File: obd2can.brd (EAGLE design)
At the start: 34.6 x 29.1 mm, 18 parts, among them Q1 16MHz, SW3 6X3.5_TACT, U2 SN65HVD235DR, U3 STM32F030XTSSOP20, U4 MCP1700, X1 RJ45_RIGHT_ANGLEMOLEX_95001-2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

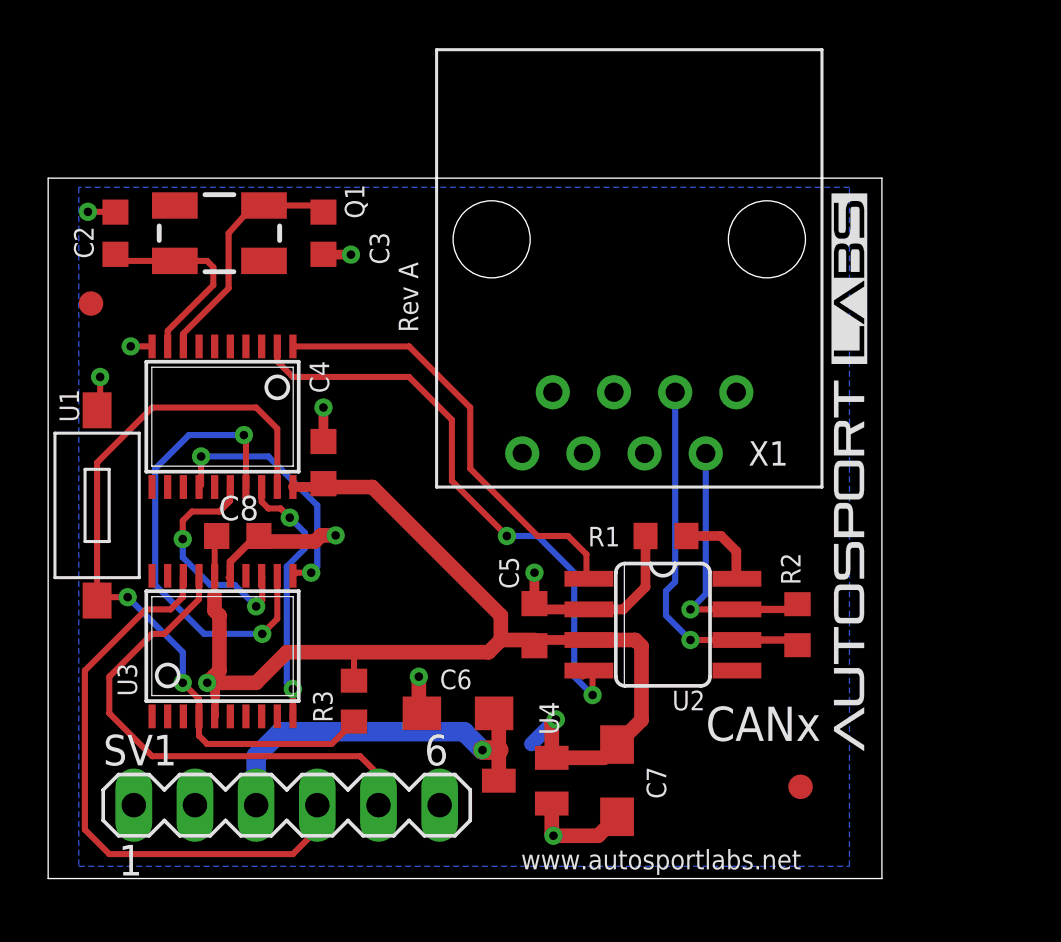
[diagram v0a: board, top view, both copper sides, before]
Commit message: added swdebug and boot button
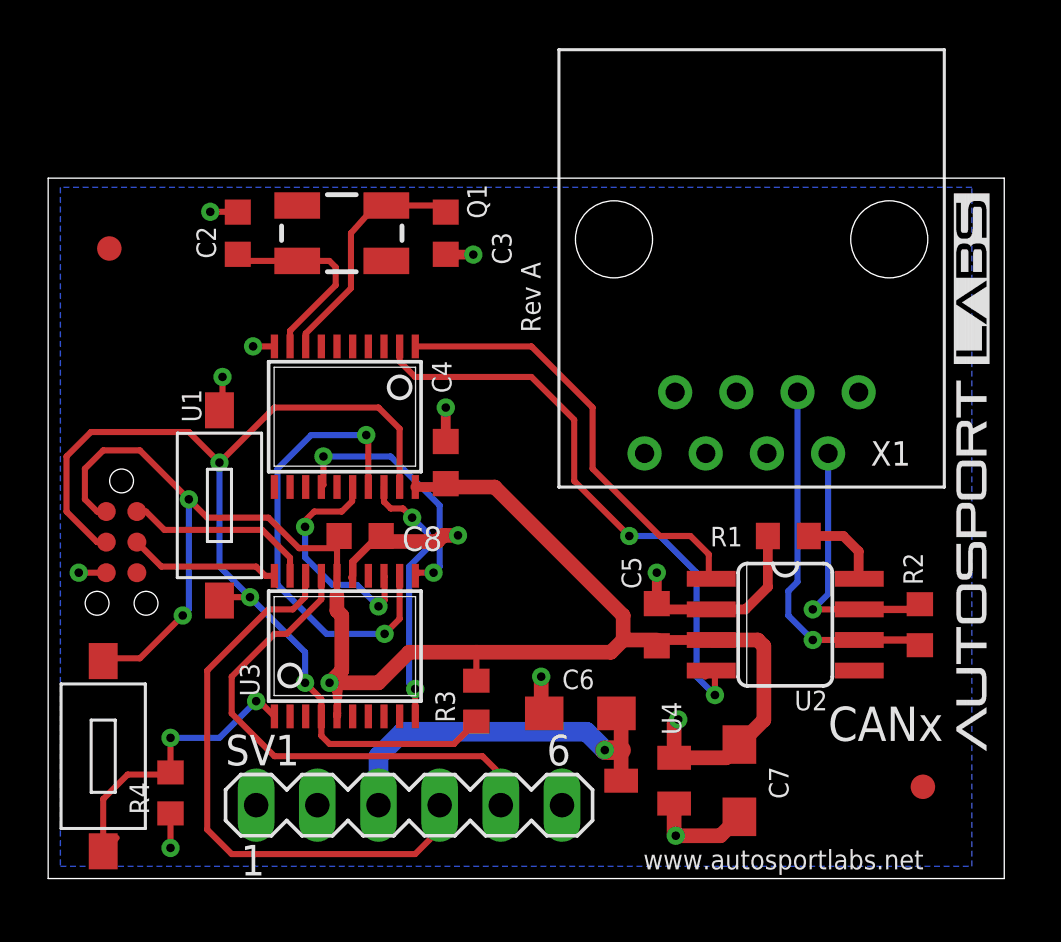
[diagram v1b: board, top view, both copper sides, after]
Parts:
- added R4: 4.7K, rcl:R0603
- added SW1: 6X3.5_TACT, tactile_switch:TACT_6X3.5
- added TC1: TC2030-IDC-NL, TagConnect:TC2030-IDC-NL
- moved C3 5.08 mm to (16.5, 26.8)
- moved C4 5.08 mm to (16.5, 17.3)
- moved C7 5.08 mm to (28.7, 4.06)
- moved R1 5.08 mm to (30.7, 14.2)
- moved R2 5.08 mm to (36.2, 10.5)
- moved R3 5.08 mm to (17.8, 7.37)
- moved X1 5.08 mm to (29.2, 26.5)
- moved C8 5.08 mm to (13.0, 14.2)
- moved U1 5.08 mm to (12.3, 19.2)
- moved U3 5.08 mm to (12.3, 9.65)
- moved C2 5.08 mm to (7.87, 26.8)
- moved Q1 5.08 mm to (12.2, 26.8)
- moved SV1 5.08 mm to (15.0, 3.05)
- moved SW3 5.08 mm to (7.11, 15.5)
- moved C5 5.08 mm to (25.3, 10.5)
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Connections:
- new net BOOT0: R4.2, SW1.P$1, U3.1
- new net SWCLK: TC1.4, U3.20
- new net SWDIO: TC1.2, U3.19
- net GND: now also R4.1, TC1.5
- net RESET: now also TC1.3
- net V+: now also SW1.P$2, TC1.1
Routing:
- net V+: track 50.9 -> 73.6 mm, vias 2 -> 4
- net BOOT0: track 0.00 -> 12.9 mm, vias 0 -> 2
- net RESET: track 32.2 -> 44.4 mm, vias 2 -> 3
- net SWDIO: track 0.00 -> 7.91 mm
- net SWCLK: track 0.00 -> 6.29 mm
- net GND: track 26.4 -> 29.2 mm, vias 9 -> 11
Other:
- board size 34.6 x 29.1 mm -> 39.7 x 29.1 mm

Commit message: minor label updates
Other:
- board text added: "OBD2CAN"
- board text removed: "CANx"
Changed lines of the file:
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@@
 <wire x1="39.7002" y1="29.083" x2="0" y2="29.083" width="0" layer="20"/>
 <wire x1="0" y1="29.083" x2="0" y2="0" width="0" layer="20"/>
-<text x="24.7142" y="0.381" size="0.8128" layer="21" font="vector">www.autosportlabs.net</text>
+<text x="11.2522" y="0.381" size="0.8128" layer="21" font="vector">www.autosportlabs.net</text>
 <text x="20.447" y="22.6822" size="0.8128" layer="21" font="vector" rot="R90">Rev A</text>
-<text x="32.385" y="5.715" size="1.4224" layer="21">CANx</text>
+<text x="29.845" y="1.397" size="1.4224" layer="21">OBD2CAN</text>
 <rectangle x1="35.5422" y1="24.9022" x2="42.6288" y2="24.9148" layer="21" rot="R90"/>
 <rectangle x1="35.5295" y1="24.9022" x2="42.6161" y2="24.9148" layer="21" rot="R90"/>

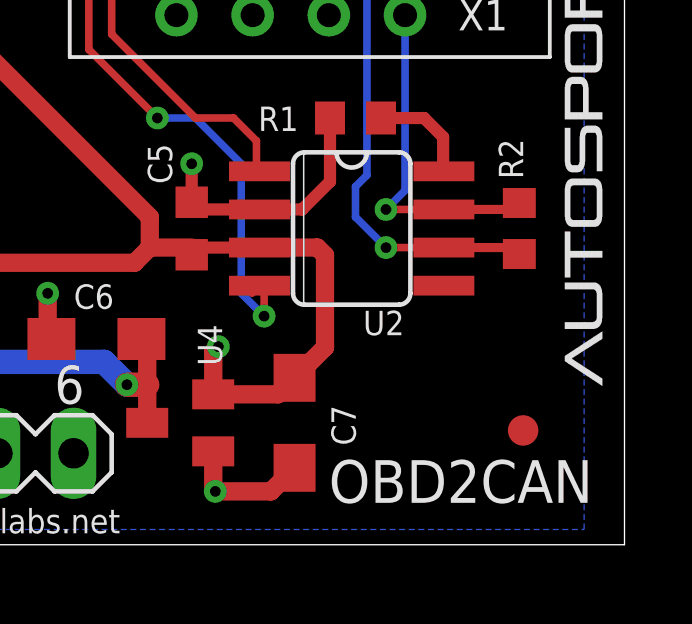
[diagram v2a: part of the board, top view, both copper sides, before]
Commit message: grounded vref pin on can transceiver
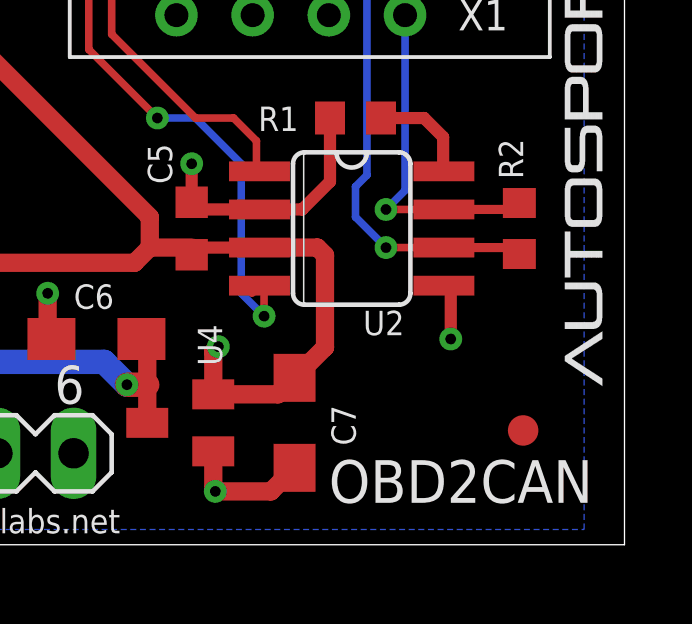
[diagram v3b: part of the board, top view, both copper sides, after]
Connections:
- net GND: now also U2.5
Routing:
- net GND: track 29.2 -> 31.2 mm, vias 11 -> 12
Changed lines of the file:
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@@
 <via x="5.08" y="1.27" extent="1-16" drill="0.3556"/>
 <wire x1="5.08" y1="1.27" x2="5.08" y2="2.706" width="0.254" layer="1"/>
+<contactref element="U2" pad="5"/>
+<via x="33.909" y="6.858" extent="1-16" drill="0.3556"/>
+<wire x1="33.6804" y1="8.636" x2="33.909" y2="8.636" width="0.4064" layer="1"/>
+<wire x1="33.909" y1="8.636" x2="33.909" y2="6.858" width="0.4064" layer="1"/>
 </signal>
 <signal name="+5V">

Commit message: OBD2CAN WIP
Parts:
- removed C4: 0.1uF, rcl:C0603K
- removed C6: 10uF, rcl:SMC_A
- removed C8: 0.1uf, rcl:C0603K
- removed SW1, SW3: 6X3.5_TACT, tactile_switch:TACT_6X3.5
- removed TC1: TC2030-IDC-NL, TagConnect:TC2030-IDC-NL
- removed U4: MCP1700, mcp1700:SOT-23
- added C10: 1uf, rcl:C0603K
- added C11: 0.01uf, rcl:C0603K
- added C12, C15: 4.7uf, rcl:C0603K
- added C14, C9: 0.1uf, rcl:C0603K
- added C25, C28: 22uF, rcl:C1206
- added C27: 10nF, rcl:C0603
- added D1: SCHOTTKY, smt_diodes:SMA
- added D2: 400V 1A, smt_diodes:SMA
- added D5: (no value), diode:SMC
- added L1: 4.7uH, rcl:L2012C
- added L2: (no value), wuerth-elektronik:1812
- added R5: 4.7K, rcl:R0603
- added SW2: 6X3.5_TACT, tactile_switch:TACT_6X3.5
- added TC2: TC2030-IDC-NL, TagConnect:TC2030-IDC-NL
- added TP2: TPB1,27, testpad:B1,27
- added X2: RJ45_RIGHT_ANGLEMOLEX_95001-2881, FCI_RJ12:RJ45_RIGHT_ANGLE_MOLEX_95001-2881
- C2, C3: value 22pF -> 33pF; device rcl:C0603K -> SparkFun:0603
- Q1: value 16MHz -> 8MHz; device SparkFun:CRYSTAL-SMD-5X3 -> SparkFun2:CRYSTAL-SMD-5X3
- R3: value 4.7K -> 16.2K 1%
- R4: value 4.7K -> 49.9K 1%
- U1: value (none) -> AP3211KTR-G1; device can:TSSOP20 -> diodes_inc:SOT-23-6
- U3: value STM32F030XTSSOP20 -> STM32F072-LQFP48; device stm32f030x:TSSOP-20 -> stm32f0:LQFP48
- moved C2 32.8 mm to (40.4, 22.6), turned to 0 degrees
- moved SV1 29.4 mm to (8.64, 31.8)
- moved Q1 27.4 mm to (38.6, 19.6), turned to 0 degrees
- moved C7 26.1 mm to (24.1, 29.7), turned to 0 degrees
- moved X1 26.0 mm to (3.94, 20.3), turned to 270 degrees
- moved C3 26.0 mm to (40.4, 16.5), turned to 180 degrees
- moved R2 23.4 mm to (19.9, 27.3), turned to 0 degrees
- moved U3 20.5 mm to (29.7, 20.6), turned to 180 degrees
- moved R4 17.0 mm to (20.3, 11.2), turned to 270 degrees
- moved R1 16.4 mm to (16.3, 21.8), turned to 90 degrees
- moved U2 15.5 mm to (19.9, 21.7), turned to 0 degrees
- moved U1 14.5 mm to (21.3, 7.87), turned to 90 degrees
- moved C5 7.91 mm to (19.9, 16.4), turned to 180 degrees
- moved R3 5.95 mm to (22.4, 11.2)
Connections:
- removed net BOOT0: R4.2, SW1.P$1, U3.1
- removed net CAN1_RX: U1.2, U2.4
- removed net CAN1_TX: U1.1, U2.1
- removed net MISO: U1.17, U3.12
- removed net MOSI: U1.16, U3.13
- removed net N$2: C3.1, Q1.1, U1.8
- removed net NPCS1: U1.18, U3.10
- removed net SPCK: U1.14, U3.11
- removed net UART1_RX: SV1.4, U3.18
- removed net UART1_TX: SV1.5, U3.17
- new net +12V: L2.2, X1.P8, X2.P8
- new net AGND: U3.8
- new net ANALOG_1_ADC: U3.10
- new net CAN_RX: U2.4, U3.32
- new net CAN_TX: U2.1, U3.33
- new net N$3: TP2.TP, U3.18
- new net N$40: C2.2, Q1.3, U3.6
- new net N$42: C3.2, Q1.1, U3.5
- new net N$5: C27.2, U1.1
- new net N$50: D2.A, L2.1
- new net N$6: C27.1, D1.C, L1.1, U1.6
- new net SAFE12V: C25.1, D2.C, D5.C, U1.4, U1.5
- new net U3: R4.1, R5.2, TC2.1
- new net USART1_RX: SV1.4, U3.31
- new net USART1_TX: SV1.5, U3.30
- new net USART2_RX: U3.13
- new net USART2_TX: U3.12
- net +5V: no longer C6.+, U4.3
- net GND: now also C10.2, C11.2, C12.2, C14.2, C15.2, C2.1, C25.2, C28.2, C3.1, C9.2, D1.A, D5.A, R3.2, SW2.P$2, TC2.5, U1.2, U3.23, U3.35, U3.44, U3.47, X2.P1; no longer C2.2, C3.2, C4.2, C6.-, C8.2, R4.1, SW3.P$2, TC1.5, U1.10, U3.15, U4.1
- net N$1: now also R3.1, R4.2, U1.3; no longer C2.1, Q1.3, U1.9
- net RESET: now also R5.1, SW2.P$1, TC2.3, U3.7; no longer R3.1, SW3.P$1, TC1.3, U1.19, U3.4
- net SWCLK: now also TC2.4, U3.37; no longer TC1.4, U3.20
- net SWDIO: now also TC2.2, U3.34; no longer TC1.2, U3.19
- net V+: now also C10.1, C11.1, C12.1, C14.1, C15.1, C28.1, C9.1, L1.2, U3.1, U3.24, U3.36, U3.48, U3.9; no longer C4.1, C8.1, R3.2, SW1.P$2, TC1.1, U1.20, U3.16, U3.5, U4.2
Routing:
- net V+: track 73.6 -> 2.29 mm, vias 4 -> 0
- net RESET: track 44.4 -> 0.00 mm, vias 3 -> 0
- net CAN1_RX: track 24.9 -> 0.00 mm, vias 2 -> 0
- net UART1_RX: track 24.3 -> 0.00 mm
- net GND: track 31.2 -> 8.15 mm, vias 12 -> 2
- net UART1_TX: track 21.1 -> 0.00 mm
- net MISO: track 19.4 -> 0.00 mm, vias 2 -> 0
- net CAN1_TX: track 18.3 -> 0.00 mm
- net +5V: track 15.8 -> 0.00 mm, vias 1 -> 0
- net BOOT0: track 12.9 -> 0.00 mm, vias 2 -> 0
- net NPCS1: track 11.0 -> 0.00 mm, vias 2 -> 0
- net SPCK: track 10.7 -> 0.00 mm, vias 2 -> 0
- net N$2: track 10.0 -> 0.00 mm
- net MOSI: track 9.68 -> 0.00 mm, vias 2 -> 0
- net N$1: track 8.41 -> 0.00 mm
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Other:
- board size 39.7 x 29.1 mm -> 96.5 x 40.6 mm

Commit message: combined designs together
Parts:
- removed C25, C28: 22uF, rcl:C1206
- removed C27: 10nF, rcl:C0603
- removed D5: (no value), diode:SMC
- removed L1: 4.7uH, rcl:L2012C
- removed L2: (no value), wuerth-elektronik:1812
- removed Q1: 8MHz, SparkFun2:CRYSTAL-SMD-5X3
- removed SV1: (no value), con-lstb:MA06-1
- removed SW2: 6X3.5_TACT, tactile_switch:TACT_6X3.5
- removed TC2: TC2030-IDC-NL, TagConnect:TC2030-IDC-NL
- removed TP2: TPB1,27, testpad:B1,27
- removed X1: RJ45_RIGHT_ANGLEMOLEX_95001-2881, FCI_RJ12:RJ45_RIGHT_ANGLE_MOLEX_95001-2881
- added C1, C17, C6: 1uF, SparkFun:0402-CAP
- added C1000: 10uF, rcl:SMC_A
- added C10000: 1uf, rcl:C0603K
- added C11000, C13000: 22uF, rcl:C1206
- added C13: 560pF, SparkFun:0402-CAP
- added C16: 470pF, SparkFun:0402-CAP
- added C18: 10uF, SparkFun:EIA3216
- added C19: 10nF, rcl:C0603
- added C2000, C6000, C9000: 0.1uf, rcl:C0603K
- added C3000, C7000: 4.7uf, rcl:C0603K
- added C4: 10uF ESR<=5, SparkFun:EIA3216
- added C4000: 0.01uf, rcl:C0603K
- added C8: 4.7uF, SparkFun:0402-CAP
- added D1000: (no value), diode:SMC
- added D2000: 400V 1A, smt_diodes:SMA
- added D3: BAS16, SparkFun:SOD-323
- added D3000: SCHOTTKY, smt_diodes:SMA
- added D4: MBRA140, SparkFun:SMA-DIODE
- added IC1: SCANTOOL, SparkFun:_STN_SCANTOOL_QFN-28-S
- added IC3: LM339PWR, _stn_logic:TSSOP-14
- added IC4: MCP2551, _stn_microchip:SO-8
- added JP1: (no value), SparkFun:1X08
- added JP8: DNP, SparkFun:FTDI_BASIC
- added JP9: DNP, SparkFun:1X02
- added L1000: (no value), wuerth-elektronik:1812
- added L2000: 4.7uH, rcl:L2012C
- added LED1, LED3: YELLOW, SparkFun:LED-0603
- added LED2, LED4, LED5: RED, SparkFun:LED-0603
- added Q10, Q9: BSS138, SparkFun:SOT23-3
- added Q1000: 8MHz, SparkFun2:CRYSTAL-SMD-5X3
- added Q3, Q4, Q8: MMBT2222, SparkFun:SOT23-3
- added Q7: ZXMP6A13FTA, SparkFun:SOT23
- added R10, R12, R18, R21, R27, R28, R29, R30, R31, R33, R9: 10k, SparkFun:0402-RES
- added R1000: 120, rcl:R0603
- added R11, R8: 510 0.5W, _stn_rcl:2010
- added R13, R32, R7: 1k, SparkFun:0402-RES
- added R14, R15: 100, SparkFun:0402-RES
- added R16, R23, R25: 4.7k, SparkFun:0402-RES
- added R17: 1.2k, SparkFun:0402-RES
- added R19: 866, SparkFun:0402-RES
- added R20: 240, SparkFun:0402-RES
- added R22: 374, SparkFun:0402-RES
- added R24, R34: 1.5k, SparkFun:0402-RES
- added R26, R5000: 4.7K, rcl:R0603
- added R3000: 49.9K 1%, rcl:R0603
- added R35, R37: 330, SparkFun:0402-RES
- added R4000: 16.2K 1%, rcl:R0603
- added R6: 10K, SparkFun:0402-RES
- added SV1000: (no value), con-lstb:MA06-1
- added SW1: 6X3.5_TACT, tactile_switch:TACT_6X3.5
- added TC1000: TC2030-IDC-NL, TagConnect:TC2030-IDC-NL
- added U1000: SN65HVD235DR, can:SO08
- added U2000: STM32F072-LQFP48, stm32f0:LQFP48
- added U3000: AP3211KTR-G1, diodes_inc:SOT-23-6
- added X1000, X2000: RJ45_RIGHT_ANGLEMOLEX_95001-2881, FCI_RJ12:RJ45_RIGHT_ANGLE_MOLEX_95001-2881
- added Y1: 16MHz, SparkFun:CRYSTAL-SMD-5X3
- C10: value 1uf -> 0.1uF; device rcl:C0603K -> SparkFun:0402-CAP
- C11: value 0.01uf -> 1uF; device rcl:C0603K -> SparkFun:0402-CAP
- C12: value 4.7uf -> 560pF; device rcl:C0603K -> SparkFun:0402-CAP
- C14: value 0.1uf -> 0.1uF; device rcl:C0603K -> SparkFun:0402-CAP
- C15: value 4.7uf -> 2.2uF; device rcl:C0603K -> SparkFun:0402-CAP
- C2, C3: value 33pF -> 27pF; device SparkFun:0603 -> SparkFun:0402-CAP
- C5: value 0.1uf -> 1uF; device rcl:C0603K -> SparkFun:0402-CAP
- C7: value 10uF -> 0.1uF; device rcl:SMC_A -> SparkFun:0402-CAP
- C9: value 0.1uf -> 10uF; device rcl:C0603K -> SparkFun:EIA3216
- D1: value SCHOTTKY -> BAS16; device smt_diodes:SMA -> SparkFun:SOD-323
- D2: value 400V 1A -> BAS16; device smt_diodes:SMA -> SparkFun:SOD-323
- R1: value 4.7K -> 10k; device rcl:R0603 -> SparkFun:0402-RES
- R2: value 120 -> 1k; device rcl:R0603 -> SparkFun:0402-RES
- R3: value 16.2K 1% -> 62K; device rcl:R0603 -> SparkFun:0402-RES
- R4: value 49.9K 1% -> 330; device rcl:R0603 -> SparkFun:0402-RES
- R5: value 4.7K -> 330; device rcl:R0603 -> SparkFun:0402-RES
- U1: value AP3211KTR-G1 -> 3.3V; device diodes_inc:SOT-23-6 -> SparkFun:SOT23-5
- U2: value SN65HVD235DR -> V_REG_317DPACK; device can:SO08 -> SparkFun:V-REG_DPACK
- U3: value STM32F072-LQFP48 -> 5V Reg.; device stm32f0:LQFP48 -> SparkFun:SOT23-5
- X2: value RJ45_RIGHT_ANGLEMOLEX_95001-2881 -> Male DB9; device FCI_RJ12:RJ45_RIGHT_ANGLE_MOLEX_95001-2881 -> SparkFun:DB9_MALE
- moved X2 60.4 mm to (34.3, 35.6), turned to 0 degrees
- moved U1 44.2 mm to (63.5, 21.1), turned to 180 degrees
- moved C2 37.1 mm to (3.81, 16.5), turned to 270 degrees
- moved U3 34.7 mm to (63.5, 12.7), turned to 270 degrees
- moved C3 34.4 mm to (6.35, 11.4)
- moved C12 32.5 mm to (57.1, 17.8), turned to 270 degrees
- moved C10 29.9 mm to (63.5, 6.73)
- moved C9 29.8 mm to (63.5, 8.89), turned to 180 degrees
- moved C15 28.4 mm to (63.5, 15.9), turned to 180 degrees
- moved C14 19.6 mm to (6.35, 29.2), turned to 180 degrees
- moved R2 18.7 mm to (2.54, 34.3), turned to 270 degrees
- moved C7 16.2 mm to (10.2, 21.6), turned to 90 degrees
- moved R3 15.1 mm to (11.4, 21.6)
- moved U2 14.5 mm to (12.7, 34.3)
- moved D2 12.5 mm to (22.9, 10.2), turned to 90 degrees
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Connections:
- new net !ISO_K_TX: IC1.22, R13.2
- new net !ISO_L_TX: IC1.23, R7.2
- new net !ISO_RX: IC1.8, IC3.2, R9.1
- new net !OBD_RX_STATUS!/PGC: IC1.19, R4.1
- new net !PWR_SAVE: IC1.15
- new net !VPW_RX: IC1.1, IC3.14, R18.1
- new net 3.3V: C1.1, C5.1, C8.1, IC1.10, IC1.25, LED1.A, LED2.A, LED3.A, LED4.A, R18.2, R27.2, R9.2, U1.5
- new net 5V: C11.1, C15.1, C18.A, C6.1, D3.2, IC4.3, R1.2, R17.2, R25.1, R34.1, U1.1, U1.3, U3.5
- new net BATT_V: C7.1, IC1.27, R3.1, R6.2
- new net CAN_HI: IC4.7, JP1.6, R14.2, X2.3
- new net CAN_LO: IC4.6, JP1.7, R15.2, X2.5
- new net HOST_PRESENT: IC1.9
- new net J1850BUS+: D1.1, JP1.3, R21.1, R28.1, R30.1, X2.7
- new net J1850BUS+_TX: IC1.3, Q9.1
- new net J1850BUS-: JP1.2, Q8.3, R29.1, R31.2, X2.6
- new net J1850BUS-_TX: IC1.4, R32.1
- new net K-LINE: JP1.5, Q4.3, R11.2, R12.1, X2.4
- new net L-LINE: JP1.4, Q3.3, R8.2, X2.8
- new net N$10: C12.1, R14.1
- new net N$11: IC4.8, R16.2
- new net N$12: IC3.9, R17.1, R23.2
- new net N$13: IC3.4, R12.2
- new net N$14: D3.1, R31.1
- new net N$15: R26.2, U1000.8
- new net N$16: R3000.2, R4000.1, U3000.3
- new net N$17: C19.2, U3000.1
- new net N$18: Q7.1, Q9.3, R24.2
- new net N$19: C19.1, D3000.C, L2000.1, U3000.6
- new net N$22: Q10.3, R19.1, R22.2
- new net N$24: D2.2, R30.2
- new net N$25: Q8.1, R32.2
- new net N$26: C4.A, IC1.17
- new net N$27: C13.1, R15.1
- new net N$30: LED3.C, R4.2
- new net N$31: LED4.C, R5.1
- new net N$32: LED5.A, R2.1
- new net N$35: LED1.C, R35.2
- new net N$36: LED2.C, R37.1
- new net N$4: Q4.1, R13.1
- new net N$7: IC3.8, R21.2
- new net N$8: R19.2, R20.2, U2.1
- new net N$9: D1.2, Q7.3
- new net OSC1: C2.1, IC1.6, Y1.3
- new net OSC2: C3.1, IC1.7, Y1.1
- new net PWM/!VPW: IC1.28, Q10.1
- new net PWM_RX: IC1.2, IC3.1, R27.1
- new net RST_NVM: IC1.18, JP9.1, R5.2
- new net RX-I: IC1.13, JP8.TXO
- new net RX-STAT: IC1.21, R35.1
- new net TX-O: IC1.14, JP8.RXI, R25.2
- new net TX-STAT: IC1.20, R37.2
- new net VBAT: C14.1, D4.C, IC3.3, JP1.8, R10.1, R11.1, R8.1, U2.3
- new net VBATT_RAW: D4.A, R3.2, X2.9
- new net VCC: C10.1, C17.1, C9.A, Q7.2, R2.2, R20.1, R24.1, U2.4, U3.1, U3.3
- net +12V: now also L1000.2, X1000.P8, X2000.P8; no longer L2.2, X1.P8, X2.P8
- net +5V: now also SV1000.3; no longer SV1.3
- net AGND: now also U2000.8; no longer U3.8
- net ANALOG_1_ADC: now also U2000.10; no longer U3.10
- net CANH: now also R1000.1, U1000.7, X1000.P2; no longer R2.1, U2.7, X1.P2
- net CANL: now also R1000.2, U1000.6, X1000.P3; no longer R2.2, U2.6, X1.P3
- net CAN_RX: now also IC1.11, IC4.4, U1000.4, U2000.32; no longer U2.4, U3.32
- net CAN_TX: now also IC1.12, IC4.1, R34.2, U1000.1, U2000.33; no longer U2.1, U3.33
- net GND: now also C1.2, C1000.-, C10000.2, C11000.2, C13.2, C13000.2, C16.2, C17.2, C18.C, C2.2, C2000.2, C3.2, C3000.2, C4.C, C4000.2, C6.2, C6000.2, C7.2, C7000.2, C8.2, C9.C, C9000.2, D1000.A, D2.1, D3000.A, IC1.16, IC1.24, IC1.5, IC1.EXP, IC3.12, IC4.2, JP1.1, JP8.GND, JP9.2, LED5.C, Q10.2, Q3.2, Q4.2, Q8.2, Q9.2, R16.1, R22.1, R23.1, R26.1, R33.2, R4000.2, R6.1, SV1000.1, SW1.P$2, TC1000.5, U1000.2, U1000.5, U2000.23, U2000.35, U2000.44, U2000.47, U3.2, U3000.2, X1000.P1, X2.1, X2.2, X2000.P1; no longer C2.1, C25.2, C28.2, C3.1, C7.-, C9.2, D1.A, D5.A, R1.1, R3.2, SV1.1, SW2.P$2, TC2.5, U2.2, U2.5, U3.23, U3.35, U3.44, U3.47, X1.P1, X2.P1
- net N$1: now also IC3.7, R28.2; no longer R3.1, R4.2, U1.3
- net N$3: now also IC3.6, R29.2; no longer TP2.TP, U3.18
- net N$34: now also C16.1, U3.4; no longer R1.2, U2.8
- net N$40: now also Q1000.3, U2000.6; no longer C2.2, Q1.3, U3.6
- net N$42: now also Q1000.1, U2000.5; no longer C3.2, Q1.1, U3.5
- net N$5: now also Q3.1, R7.1; no longer C27.2, U1.1
- net N$50: now also D2000.A, L1000.1; no longer D2.A, L2.1
- net N$6: now also IC3.5, R10.2, R33.1; no longer C27.1, D1.C, L1.1, U1.6
- net RESET: now also IC1.26, R1.1, R5000.1, SW1.P$1, TC1000.3, U2000.7; no longer R5.1, SW2.P$1, TC2.3, U3.7
- net SAFE12V: now also C11000.1, D1000.C, D2000.C, U3000.4, U3000.5; no longer C25.1, D2.C, D5.C, U1.4, U1.5
- net SWCLK: now also TC1000.4, U2000.37; no longer TC2.4, U3.37
- net SWDIO: now also TC1000.2, U2000.34; no longer TC2.2, U3.34
- net U3: now also R3000.1, R5000.2, TC1000.1; no longer R4.1, R5.2, TC2.1
- net USART1_RX: now also SV1000.4, U2000.31; no longer SV1.4, U3.31
- net USART1_TX: now also SV1000.5, U2000.30; no longer SV1.5, U3.30
- net USART2_RX: now also U2000.13; no longer U3.13
- net USART2_TX: now also U2000.12; no longer U3.12
- net V+: now also C1000.+, C10000.1, C13000.1, C2000.1, C3000.1, C4000.1, C6000.1, C7000.1, C9000.1, L2000.2, U1000.3, U2000.1, U2000.24, U2000.36, U2000.48, U2000.9; no longer C10.1, C11.1, C12.1, C14.1, C15.1, C28.1, C5.1, C7.+, C9.1, L1.2, U2.3, U3.1, U3.24, U3.36, U3.48, U3.9
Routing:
- net VCC: track 0.00 -> 129.3 mm, vias 0 -> 22
- net 5V: track 0.00 -> 124.3 mm, vias 0 -> 6
- net 3.3V: track 0.00 -> 98.1 mm, vias 0 -> 6
- net VBAT: track 0.00 -> 90.1 mm, vias 0 -> 8
- net K-LINE: track 0.00 -> 67.2 mm, vias 0 -> 1
- net !ISO_K_TX: track 0.00 -> 47.9 mm, vias 0 -> 2
- net J1850BUS+: track 0.00 -> 47.7 mm, vias 0 -> 2
- net !ISO_L_TX: track 0.00 -> 47.4 mm, vias 0 -> 2
- net CAN_RX: track 0.36 -> 42.5 mm, vias 0 -> 2
- net J1850BUS-: track 0.00 -> 41.7 mm, vias 0 -> 1
- net CAN_LO: track 0.00 -> 41.3 mm
- net !VPW_RX: track 0.00 -> 40.3 mm, vias 0 -> 2
- net !ISO_RX: track 0.00 -> 39.5 mm, vias 0 -> 2
- net CAN_TX: track 0.00 -> 39.3 mm, vias 0 -> 2
- net L-LINE: track 0.00 -> 39.2 mm
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- added copper zone on layer 1, net GND
- added copper zone on layer 1, net VCC
- added copper zone on layer 16, net VCC
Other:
- board size 96.5 x 40.6 mm -> 96.5 x 87.9 mm
- board text added: "+"
- board text added: "-"
- board text added: "10/13/10"
- board text added: "BLK"
- board text added: "CAN"
- board text added: "GND"
- board text added: "GRN"
- board text added: "HI"
- board text added: "J1850"
- board text added: "K"
- board text added: "L"
- board text added: "LINE"
- board text added: "LO"
- board text added: "NC"
- board text added: "OBD-II-UART"
- board text added: "OBDRX"
- board text added: "OBDTX"
- board text added: "POWER"
- board text added: "RST_NVM"
- board text added: "RX"
- board text added: "RX-I"
- board text added: "TX"
- board text added: "TX-O"
- board text added: "VBAT"
